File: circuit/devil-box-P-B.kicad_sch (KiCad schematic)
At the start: 17 parts, among them M1 Motor_Servo, T1 BSS123, T2 BSS123, T3 BSS123, T4 IRF9540N, T5 BSS123

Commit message: add servo wire labels
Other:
- note added: "brown"
- note added: "orange"
- note added: "red"
- moved on the sheet: M1
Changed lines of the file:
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@@
 	(wire
 		(pts
-			(xy 223.52 129.54) (xy 228.6 129.54)
+			(xy 223.52 129.54) (xy 232.41 129.54)
 		)
 		(stroke
@@
 	(wire
 		(pts
-			(xy 223.52 127) (xy 228.6 127)
-		)
-		(stroke
-			(width 0)
-			(type default)
-		)
-	)
-	(wire
-		(pts
-			(xy 193.04 124.46) (xy 228.6 124.46)
+			(xy 223.52 127) (xy 232.41 127)
+		)
+		(stroke
+			(width 0)
+			(type default)
+		)
+	)
+	(wire
+		(pts
+			(xy 193.04 124.46) (xy 232.41 124.46)
 		)
 		(stroke
@@
 		)
 	)
-	(label "PB3_OC2A"
-		(at 196.85 124.46 0)
-		(fields_autoplaced yes)
+	(text "orange"
+		(exclude_from_sim no)
+		(at 227.584 123.698 0)
 		(effects
 			(font
 				(size 1.27 1.27)
 			)
-			(justify left bottom)
-		)
-	)
-	(label "GND"
-		(at 146.05 142.24 0)
-		(fields_autoplaced yes)
+		)
+	)
+	(text "brown\n"
+		(exclude_from_sim no)
+		(at 227.584 128.778 0)
 		(effects
 			(font
 				(size 1.27 1.27)
 			)
-			(justify left bottom)
-		)
-	)
-	(label "BAT+"
-		(at 52.07 40.64 0)
-		(fields_autoplaced yes)
+		)
+	)
+	(text "red"
+		(exclude_from_sim no)
+		(at 227.584 126.238 0)
 		(effects
 			(font
 				(size 1.27 1.27)
 			)
-			(justify left bottom)
-		)
-	)
-	(label "OC0B"
-		(at 196.85 109.22 0)
-		(fields_autoplaced yes)
+		)
+	)
+	(label "PB3_OC2A"
+		(at 196.85 124.46 0)
 		(effects
 			(font
@@
 		)
 	)
+	(label "GND"
+		(at 146.05 142.24 0)
+		(effects
+			(font
+				(size 1.27 1.27)
+			)
+			(justify left bottom)
+		)
+	)
+	(label "BAT+"
+		(at 52.07 40.64 0)
+		(effects
+			(font
+				(size 1.27 1.27)
+			)
+			(justify left bottom)
+		)
+	)
+	(label "OC0B"
+		(at 196.85 109.22 0)
+		(effects
+			(font
+				(size 1.27 1.27)
+			)
+			(justify left bottom)
+		)
+	)
 	(label "Vcc"
 		(at 146.05 67.31 0)
-		(fields_autoplaced yes)
 		(effects
 			(font
@@
 	(symbol
 		(lib_id "Motor:Motor_Servo")
-		(at 236.22 127 0)
+		(at 240.03 127 0)
 		(unit 1)
 		(exclude_from_sim no)
@@
 		(fields_autoplaced yes)
 		(property "Reference" "M1"
-			(at 244.5798 125.3545 0)
+			(at 248.3898 125.3545 0)
 			(effects
 				(font
@@
 		)
 		(property "Value" "Motor_Servo"
-			(at 244.5798 127.7787 0)
+			(at 248.3898 127.7787 0)
 			(effects
 				(font
@@
 		)
 		(property "Footprint" "Connector_PinHeader_2.54mm:PinHeader_1x03_P2.54mm_Vertical"
-			(at 236.22 131.826 0)
+			(at 240.03 131.826 0)
 			(effects
 				(font
@@
 		)
 		(property "Datasheet" "http://forums.parallax.com/uploads/attachments/46831/74481.png"
-			(at 236.22 131.826 0)
+			(at 240.03 131.826 0)
 			(effects
 				(font
@@
 		)
 		(property "Description" ""
-			(at 236.22 127 0)
-			(effects
-				(font
+			(at 240.03 127 0)
+			(effects
+				(font

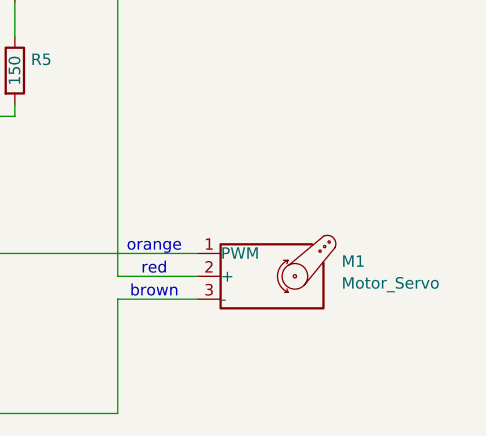
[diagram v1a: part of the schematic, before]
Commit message: change P-MOSFET to IRF9Z34N, add color labels to servo wires
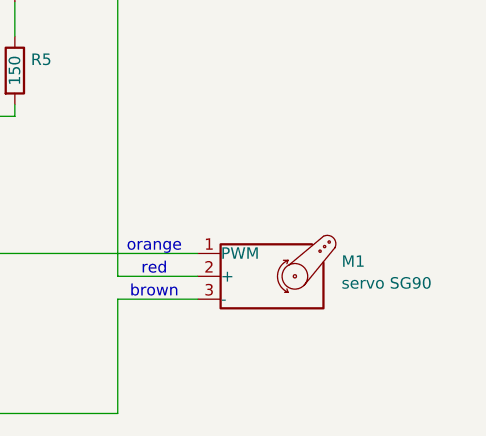
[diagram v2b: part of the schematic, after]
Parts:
- M1: value Motor_Servo -> servo SG90
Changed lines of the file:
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@@
 			)
 		)
-		(property "Value" "Motor_Servo"
+		(property "Value" "servo SG90"
 			(at 248.3898 127.7787 0)
 			(effects
